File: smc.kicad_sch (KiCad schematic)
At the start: 31 parts

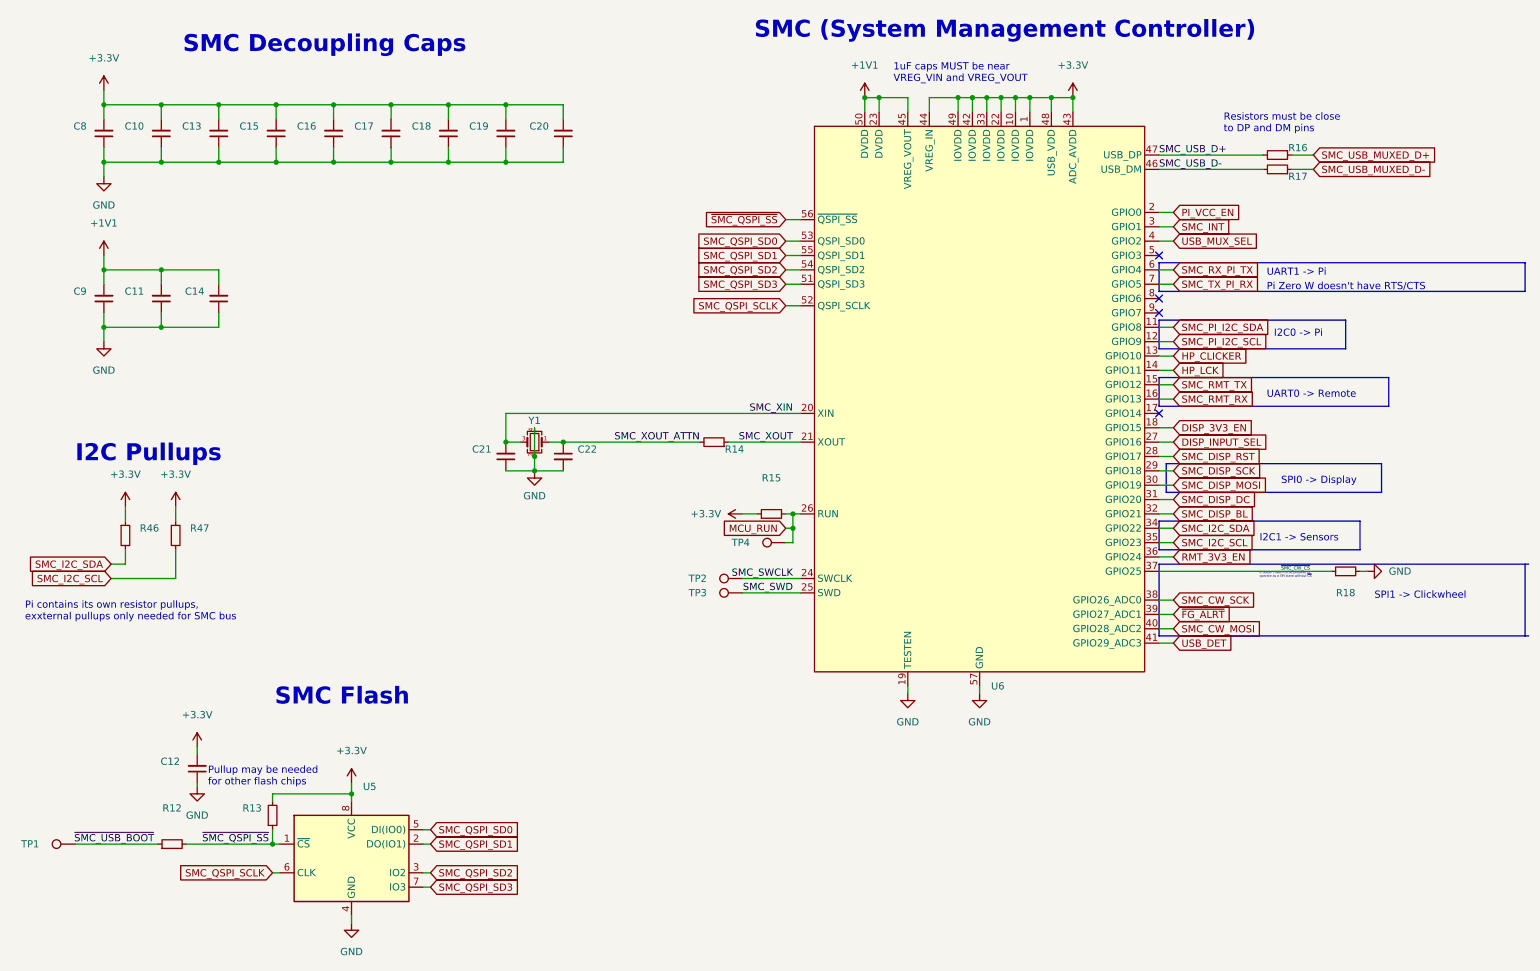
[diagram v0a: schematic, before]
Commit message: layout: add testpoints, extra mounting hole, grounding clips
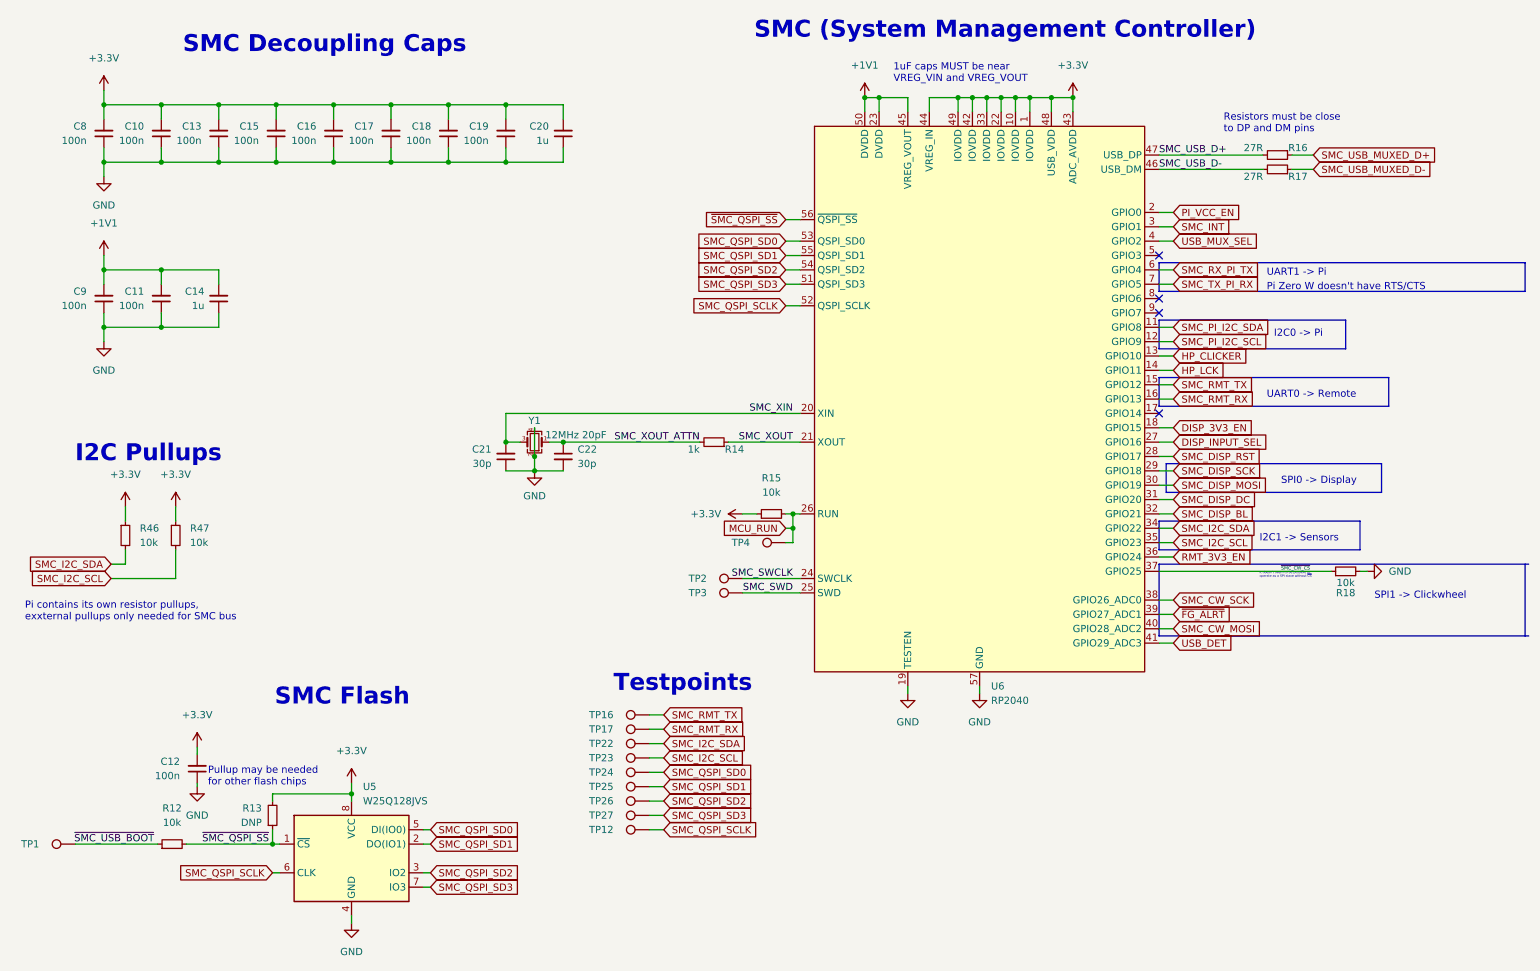
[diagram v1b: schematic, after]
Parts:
- added TP12, TP16, TP17, TP22, TP23, TP24, TP25, TP26, TP27: TestPoint, TestPoint:TestPoint_Pad_D1.5mm, symbol Connector:TestPoint
- C10, C11, C12, C13, C15, C16, C17, C18, C19, C8, C9: value (none) -> 100n; footprint (none) -> Capacitor_SMD:C_0402_1005Metric
- C14, C20: value (none) -> 1u; footprint (none) -> Capacitor_SMD:C_0402_1005Metric
- C21, C22: value (none) -> 30p; footprint (none) -> Capacitor_SMD:C_0402_1005Metric
- R12, R15, R18, R46, R47: value (none) -> 10k; footprint (none) -> Resistor_SMD:R_0402_1005Metric
- R13: value (none) -> DNP; footprint (none) -> Resistor_SMD:R_0402_1005Metric
- R14: value (none) -> 1k; footprint (none) -> Resistor_SMD:R_0402_1005Metric
- R16, R17: value (none) -> 27R; footprint (none) -> Resistor_SMD:R_0402_1005Metric
- TP1, TP2, TP3, TP4: value (none) -> TestPoint; footprint (none) -> TestPoint:TestPoint_Pad_D1.5mm
- U5: value (none) -> W25Q128JVS; footprint (none) -> Package_SON:WSON-8-1EP_6x5mm_P1.27mm_EP3.4x4.3mm
- U6: value (none) -> RP2040; footprint (none) -> Package_DFN_QFN:QFN-56-1EP_7x7mm_P0.4mm_EP5.6x5.6mm
- Y1: value (none) -> 12MHz 20pF; footprint (none) -> Crystal:Crystal_SMD_2520-4Pin_2.5x2.0mm
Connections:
- net SMC_I2C_SCL: now also TP23.1
- net SMC_I2C_SDA: now also TP22.1
- net SMC_QSPI_SCLK: now also TP12.1
- net SMC_QSPI_SD0: now also TP24.1
- net SMC_QSPI_SD1: now also TP25.1
- net SMC_QSPI_SD2: now also TP26.1
- net SMC_QSPI_SD3: now also TP27.1
- net SMC_RMT_RX: now also TP17.1
- net SMC_RMT_TX: now also TP16.1
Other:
- note added: "Testpoints"

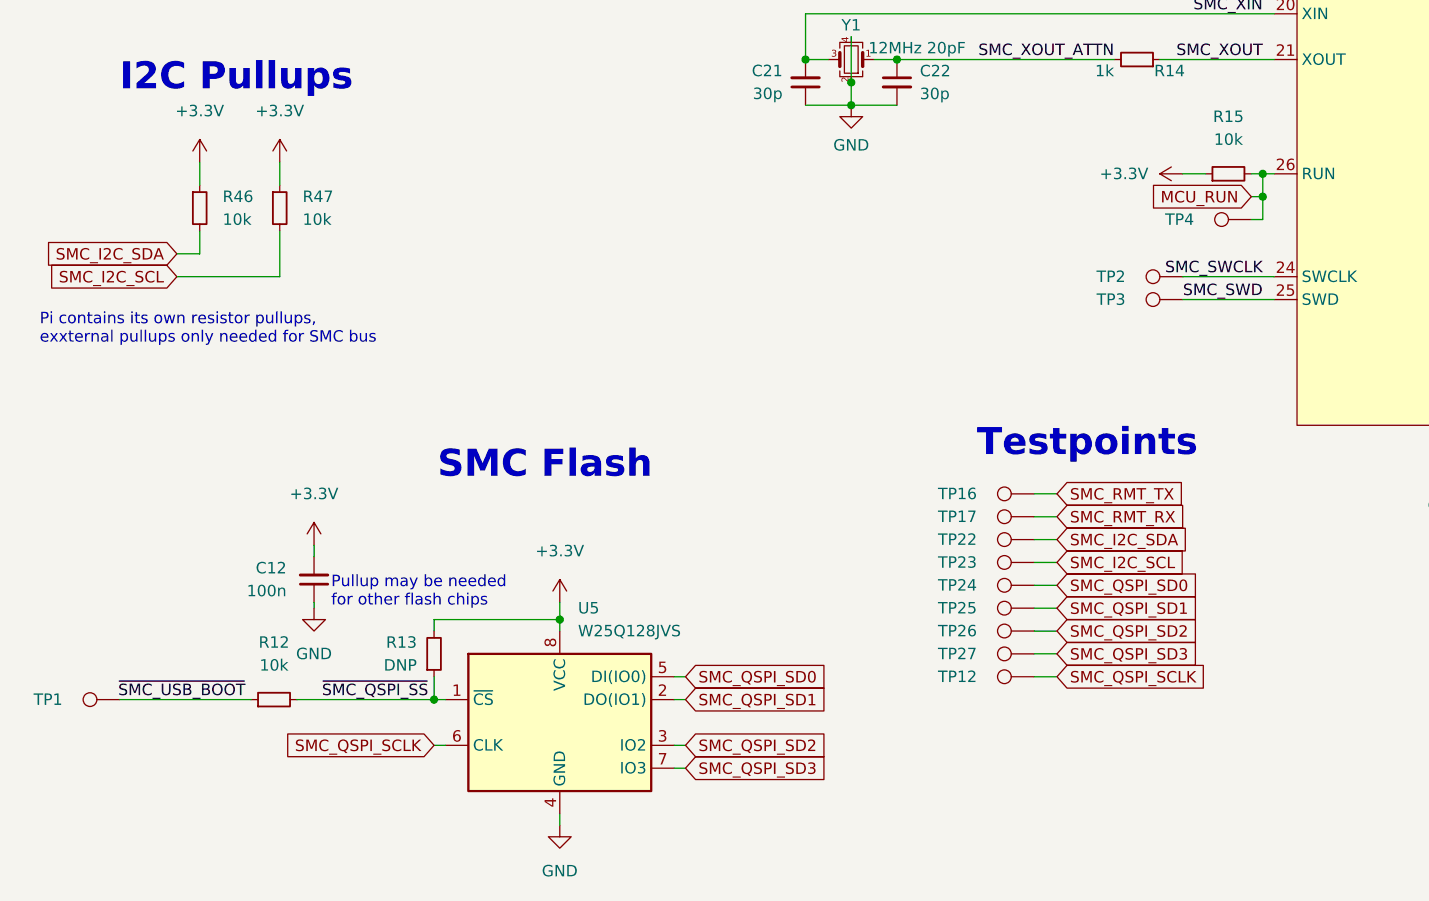
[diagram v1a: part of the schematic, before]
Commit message: layout: cleanup silkscreen, add bootloader buttons
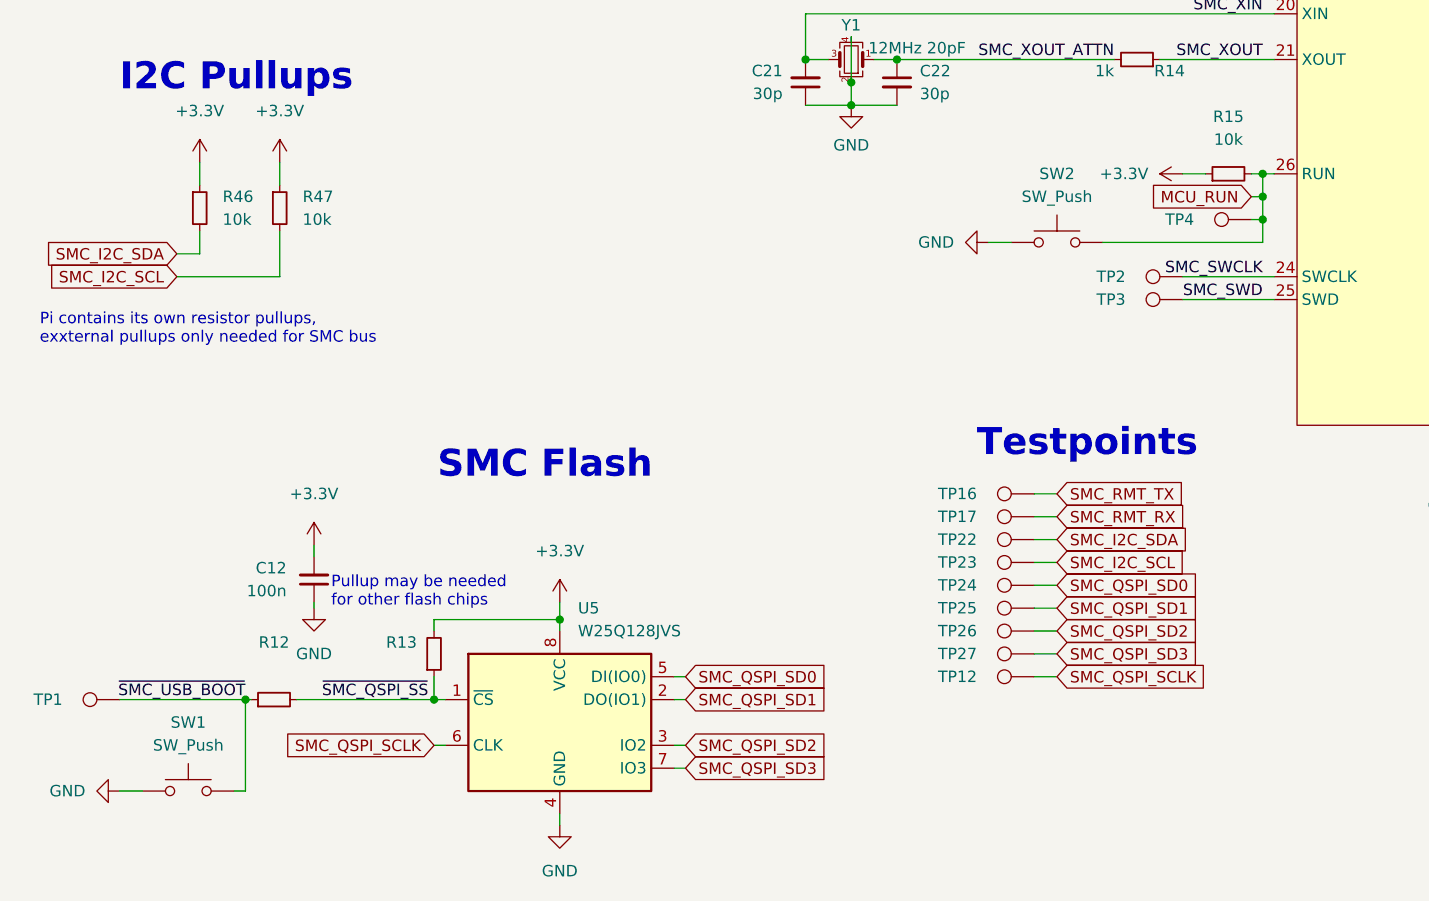
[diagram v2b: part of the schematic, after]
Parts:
- added SW1, SW2: SW_Push, symbol Switch:SW_Push
- R12: value 10k -> (none)
- R13: value DNP -> (none)
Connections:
- net GND: now also SW1.1, SW2.1
- net MCU_RUN: now also SW2.2
- net ~{SMC_USB_BOOT}: now also SW1.2
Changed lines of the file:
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@@
   (junction (at 40.64 44.45) (diameter 0) (color 0 0 0 0)
   )
+  (junction (at 152.4 121.92) (diameter 0) (color 0 0 0 0)
+  )
   (junction (at 201.93 43.18) (diameter 0) (color 0 0 0 0)
   )
   (junction (at 152.4 116.84) (diameter 0) (color 0 0 0 0)
+  )
+  (junction (at 39.37 175.26) (diameter 0) (color 0 0 0 0)
   )
   (junction (at 60.96 44.45) (diameter 0) (color 0 0 0 0)
@@
     (stroke (width 0) (type default) (color 0 0 0 0))
   )
+  (wire (pts (xy 39.37 185.42) (xy 38.1 185.42))
+    (stroke (width 0) (type default) (color 0 0 0 0))
+  )
   (polyline (pts (xy 217.17 97.79) (xy 257.81 97.79))
     (stroke (width 0) (type default) (color 0 0 0 0))
@@
     (stroke (width 0) (type default) (color 0 0 0 0))
   )
+  (wire (pts (xy 25.4 175.26) (xy 39.37 175.26))
+    (stroke (width 0) (type default) (color 0 0 0 0))
+  )
   (wire (pts (xy 217.17 119.38) (xy 219.71 119.38))
     (stroke (width 0) (type default) (color 0 0 0 0))
@@
     (stroke (width 0) (type default) (color 0 0 0 0))
   )
+  (wire (pts (xy 25.4 185.42) (xy 27.94 185.42))
+    (stroke (width 0) (type default) (color 0 0 0 0))
+  )
   (wire (pts (xy 40.64 46.99) (xy 40.64 44.45))
     (stroke (width 0) (type default) (color 0 0 0 0))
@@
     (stroke (width 0) (type default) (color 0 0 0 0))
   )
+  (wire (pts (xy 152.4 124.46) (xy 152.4 121.92))
+    (stroke (width 0) (type default) (color 0 0 0 0))
+  )
   (polyline (pts (xy 217.17 125.73) (xy 282.575 125.73))
     (stroke (width 0) (type default) (color 0 0 0 0))
@@
     (stroke (width 0) (type default) (color 0 0 0 0))
   )
+  (wire (pts (xy 39.37 175.26) (xy 40.005 175.26))
+    (stroke (width 0) (type default) (color 0 0 0 0))
+  )
   (wire (pts (xy 194.31 43.18) (xy 194.31 45.72))
     (stroke (width 0) (type default) (color 0 0 0 0))
@@
     (stroke (width 0) (type default) (color 0 0 0 0))
   )
+  (wire (pts (xy 39.37 185.42) (xy 39.37 175.26))
+    (stroke (width 0) (type default) (color 0 0 0 0))
+  )
   (wire (pts (xy 217.17 101.6) (xy 219.71 101.6))
     (stroke (width 0) (type default) (color 0 0 0 0))
@@
     (stroke (width 0) (type default) (color 0 0 0 0))
   )
-  (wire (pts (xy 25.4 175.26) (xy 40.005 175.26))
-    (stroke (width 0) (type default) (color 0 0 0 0))
-  )
   (wire (pts (xy 217.17 106.68) (xy 219.71 106.68))
     (stroke (width 0) (type default) (color 0 0 0 0))
@@
     (stroke (width 0) (type default) (color 0 0 0 0))
   )
+  (wire (pts (xy 121.92 124.46) (xy 124.46 124.46))
+    (stroke (width 0) (type default) (color 0 0 0 0))
+  )
   (wire (pts (xy 50.8 54.61) (xy 40.64 54.61))
     (stroke (width 0) (type default) (color 0 0 0 0))
@@
   )
   (polyline (pts (xy 217.17 72.39) (xy 281.94 72.39))
+    (stroke (width 0) (type default) (color 0 0 0 0))
+  )
+  (wire (pts (xy 134.62 124.46) (xy 152.4 124.46))
     (stroke (width 0) (type default) (color 0 0 0 0))
   )
@@
     (in_bom yes) (on_board yes) (fields_autoplaced)
     (property "Reference" "R12" (id 0) (at 42.545 168.91 90))
-    (property "Value" "10k" (id 1) (at 42.545 171.45 90))
+    (property "Value" "" (id 1) (at 42.545 171.45 90))
     (property "Footprint" "Resistor_SMD:R_0402_1005Metric" (id 2) (at 42.545 175.26 0)
       (effects (font (size 1.27 1.27)) hide)
@@
       (effects (font (size 1.27 1.27)) (justify right))
     )
-    (property "Value" "DNP" (id 1) (at 58.42 171.4499 0)
+    (property "Value" "" (id 1) (at 58.42 171.4499 0)
       (effects (font (size 1.27 1.27)) (justify right))
     )
@@
     (pin "1")
   )
+  (symbol (lib_id "Switch:SW_Push") (at 33.02 185.42 0) (unit 1)
+    (in_bom yes) (on_board yes) (fields_autoplaced)
+    (property "Reference" "SW1" (id 0) (at 33.02 177.8 0))
+    (property "Value" "SW_Push" (id 1) (at 33.02 180.34 0))
+    (property "Footprint" "" (id 2) (at 33.02 180.34 0)
+      (effects (font (size 1.27 1.27)) hide)
+    )
+    (property "Datasheet" "~" (id 3) (at 33.02 180.34 0)
+      (effects (font (size 1.27 1.27)) hide)
+    )
+    (pin "1")
+    (pin "2")
+  )
   (symbol (lib_id "power:+3.3V") (at 201.93 43.18 0) (unit 1)
     (in_bom yes) (on_board yes) (fields_autoplaced)
@@
     )
     (property "Datasheet" "" (id 3) (at 201.93 43.18 0)
+      (effects (font (size 1.27 1.27)) hide)
+    )
+    (pin "1")
+  )
+  (symbol (lib_id "Switch:SW_Push") (at 129.54 124.46 0) (unit 1)
+    (in_bom yes) (on_board yes) (fields_autoplaced)
+    (property "Reference" "SW2" (id 0) (at 129.54 116.84 0))
+    (property "Value" "SW_Push" (id 1) (at 129.54 119.38 0))
+    (property "Footprint" "" (id 2) (at 129.54 119.38 0)
+      (effects (font (size 1.27 1.27)) hide)
+    )
+    (property "Datasheet" "~" (id 3) (at 129.54 119.38 0)
+      (effects (font (size 1.27 1.27)) hide)
+    )
+    (pin "1")
+    (pin "2")
+  )
+  (symbol (lib_id "power:GND") (at 25.4 185.42 270) (unit 1)
+    (in_bom yes) (on_board yes) (fields_autoplaced)
+    (property "Reference" "#PWR0142" (id 0) (at 19.05 185.42 0)
+      (effects (font (size 1.27 1.27)) hide)
+    )
+    (property "Value" "GND" (id 1) (at 21.59 185.4199 90)
+      (effects (font (size 1.27 1.27)) (justify right))
+    )
+    (property "Footprint" "" (id 2) (at 25.4 185.42 0)
+      (effects (font (size 1.27 1.27)) hide)
+    )
+    (property "Datasheet" "" (id 3) (at 25.4 185.42 0)
       (effects (font (size 1.27 1.27)) hide)
     )
@@
     (pin "9")
   )
+  (symbol (lib_id "power:GND") (at 121.92 124.46 270) (unit 1)
+    (in_bom yes) (on_board yes) (fields_autoplaced)
+    (property "Reference" "#PWR0143" (id 0) (at 115.57 124.46 0)
+      (effects (font (size 1.27 1.27)) hide)
+    )
+    (property "Value" "GND" (id 1) (at 118.11 124.4599 90)
+      (effects (font (size 1.27 1.27)) (justify right))
+    )
+    (property "Footprint" "" (id 2) (at 121.92 124.46 0)
+      (effects (font (size 1.27 1.27)) hide)
+    )
+    (property "Datasheet" "" (id 3) (at 121.92 124.46 0)
+      (effects (font (size 1.27 1.27)) hide)
+    )
+    (pin "1")
+  )
   (symbol (lib_id "Device:R_Small") (at 250.19 127 90) (unit 1)
